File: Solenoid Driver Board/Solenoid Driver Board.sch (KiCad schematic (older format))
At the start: 21 parts, among them J1 BREAKOUT, J2 Solenoid, J3 RGB_LED, J4 DEBUG, J5 MAIN, Q1 IRLB8721PBF, U1 AMS1117-5.0, U2 STM8S003F3P, Y1 Crystal

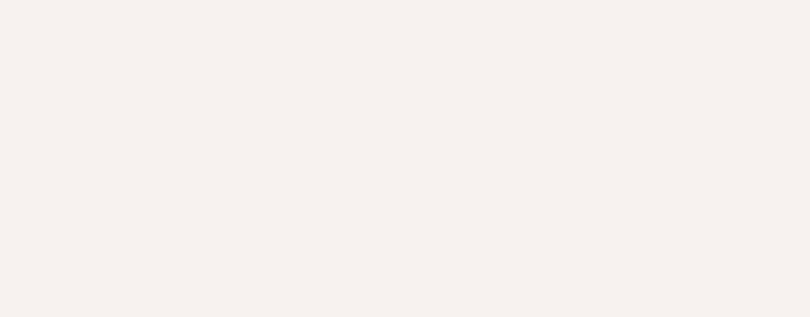
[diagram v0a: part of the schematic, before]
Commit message: Initial thoughts on protocol.  Initial board redesign notes.  Added libraries for firmware development
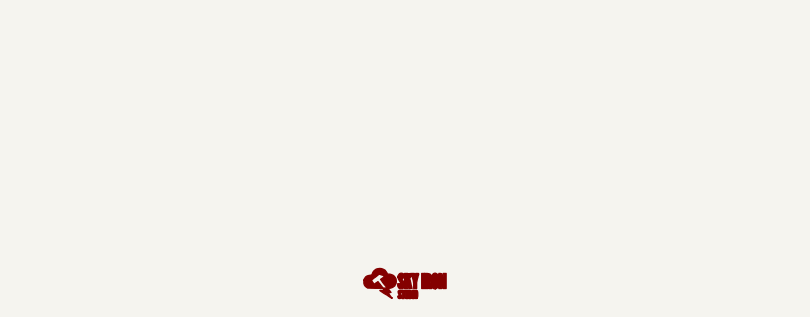
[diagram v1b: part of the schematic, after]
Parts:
- J3: footprint (none) -> Pin_Headers:Pin_Header_Straight_1x03
- R2, R4: footprint Resistors_SMD:R_0805_HandSoldering -> Resistors_SMD:R_1206_HandSoldering
- Y1: footprint Crystals:Crystal_SMD_2012-2pin_2.0x1.2mm_HandSoldering -> SpadeConnector:Crystal_HC-49-S
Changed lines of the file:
@@
 LIBS:diode
 LIBS:motors
+LIBS:SKyIronLogo
 LIBS:Solenoid Driver Board-cache
 EELAYER 25 0
@@
 $EndComp
 $Comp
-L +12V #PWR1
+L +12V #PWR01
 U 1 1 58F576B7
 P 2100 1400
-F 0 "#PWR1" H 2100 1250 50  0001 C CNN
+F 0 "#PWR01" H 2100 1250 50  0001 C CNN
 F 1 "+12V" H 2100 1540 50  0000 C CNN
 F 2 "" H 2100 1400 50  0001 C CNN
@@
 $EndComp
 $Comp
-L +5V #PWR4
+L +5V #PWR02
 U 1 1 58F576D3
 P 3100 1400
-F 0 "#PWR4" H 3100 1250 50  0001 C CNN
+F 0 "#PWR02" H 3100 1250 50  0001 C CNN
 F 1 "+5V" H 3100 1540 50  0000 C CNN
 F 2 "" H 3100 1400 50  0001 C CNN
@@
 $EndComp
 $Comp
-L GND #PWR3
+L GND #PWR03
 U 1 1 58F576F3
 P 2600 1850
-F 0 "#PWR3" H 2600 1600 50  0001 C CNN
+F 0 "#PWR03" H 2600 1600 50  0001 C CNN
 F 1 "GND" H 2600 1700 50  0000 C CNN
 F 2 "" H 2600 1850 50  0001 C CNN
@@
 	2900 1400 3500 1400
 $Comp
-L +5V #PWR6
+L +5V #PWR04
 U 1 1 58F5771C
 P 5200 1600
-F 0 "#PWR6" H 5200 1450 50  0001 C CNN
+F 0 "#PWR04" H 5200 1450 50  0001 C CNN
 F 1 "+5V" H 5200 1740 50  0000 C CNN
 F 2 "" H 5200 1600 50  0001 C CNN
@@
 $EndComp
 $Comp
-L GND #PWR7
+L GND #PWR05
 U 1 1 58F57736
 P 5200 3650
-F 0 "#PWR7" H 5200 3400 50  0001 C CNN
+F 0 "#PWR05" H 5200 3400 50  0001 C CNN
 F 1 "GND" H 5200 3500 50  0000 C CNN
 F 2 "" H 5200 3650 50  0001 C CNN
@@
 SWIM
 $Comp
-L GND #PWR18
+L GND #PWR06
 U 1 1 58F57AF4
 P 9950 1300
-F 0 "#PWR18" H 9950 1050 50  0001 C CNN
+F 0 "#PWR06" H 9950 1050 50  0001 C CNN
 F 1 "GND" H 9950 1150 50  0000 C CNN
 F 2 "" H 9950 1300 50  0001 C CNN
@@
 $EndComp
 $Comp
-L +5V #PWR17
+L +5V #PWR07
 U 1 1 58F57B17
 P 9950 1100
-F 0 "#PWR17" H 9950 950 50  0001 C CNN
+F 0 "#PWR07" H 9950 950 50  0001 C CNN
 F 1 "+5V" H 9950 1240 50  0000 C CNN
 F 2 "" H 9950 1100 50  0001 C CNN
@@
 F 0 "Y1" H 7150 2300 50  0000 C CNN
 F 1 "Crystal" H 7150 2000 50  0000 C CNN
-F 2 "Crystals:Crystal_SMD_2012-2pin_2.0x1.2mm_HandSoldering" H 7150 2150 50  0001 C CNN
+F 2 "SpadeConnector:Crystal_HC-49-S" H 7150 2150 50  0001 C CNN
 F 3 "" H 7150 2150 50  0001 C CNN
 	1    7150 2150
@@
 $EndComp
 $Comp
-L GND #PWR10
+L GND #PWR08
 U 1 1 58F57DD6
 P 7800 2150
-F 0 "#PWR10" H 7800 1900 50  0001 C CNN
+F 0 "#PWR08" H 7800 1900 50  0001 C CNN
 F 1 "GND" H 7800 2000 50  0000 C CNN
 F 2 "" H 7800 2150 50  0001 C CNN
@@
 $EndComp
 $Comp
-L GND #PWR14
+L GND #PWR09
 U 1 1 58F58125
 P 8750 4250
-F 0 "#PWR14" H 8750 4000 50  0001 C CNN
+F 0 "#PWR09" H 8750 4000 50  0001 C CNN
 F 1 "GND" H 8750 4100 50  0000 C CNN
 F 2 "" H 8750 4250 50  0001 C CNN
@@
 F 0 "R4" V 8680 4100 50  0000 C CNN
 F 1 "10K" V 8600 4100 50  0000 C CNN
-F 2 "Resistors_SMD:R_0805_HandSoldering" V 8530 4100 50  0001 C CNN
+F 2 "Resistors_SMD:R_1206_HandSoldering" V 8530 4100 50  0001 C CNN
 F 3 "" H 8600 4100 50  0001 C CNN
 	1    8600 4100
@@
 $EndComp
 $Comp
-L +12V #PWR13
+L +12V #PWR010
 U 1 1 58F5833A
 P 8750 3150
-F 0 "#PWR13" H 8750 3000 50  0001 C CNN
+F 0 "#PWR010" H 8750 3000 50  0001 C CNN
 F 1 "+12V" H 8750 3290 50  0000 C CNN
 F 2 "" H 8750 3150 50  0001 C CNN
@@
 $EndComp
 $Comp
-L +12V #PWR15
+L +12V #PWR011
 U 1 1 58F586EE
 P 9900 2050
-F 0 "#PWR15" H 9900 1900 50  0001 C CNN
+F 0 "#PWR011" H 9900 1900 50  0001 C CNN
 F 1 "+12V" H 9900 2190 50  0000 C CNN
 F 2 "" H 9900 2050 50  0001 C CNN
@@
 $EndComp
 $Comp
-L GND #PWR16
+L GND #PWR012
 U 1 1 58F58726
 P 9900 2150
-F 0 "#PWR16" H 9900 1900 50  0001 C CNN
+F 0 "#PWR012" H 9900 1900 50  0001 C CNN
 F 1 "GND" H 9900 2000 50  0000 C CNN
 F 2 "" H 9900 2150 50  0001 C CNN
@@
 F 0 "R2" V 2430 2650 50  0000 C CNN
 F 1 "10k" V 2350 2650 50  0000 C CNN
-F 2 "Resistors_SMD:R_0805_HandSoldering" V 2280 2650 50  0001 C CNN
+F 2 "Resistors_SMD:R_1206_HandSoldering" V 2280 2650 50  0001 C CNN
 F 3 "" H 2350 2650 50  0001 C CNN
 	1    2350 2650
@@
 $EndComp
 $Comp
-L +5V #PWR2
+L +5V #PWR013
 U 1 1 58FB95C2
 P 2350 2400
-F 0 "#PWR2" H 2350 2250 50  0001 C CNN
+F 0 "#PWR013" H 2350 2250 50  0001 C CNN
 F 1 "+5V" H 2350 2540 50  0000 C CNN
 F 2 "" H 2350 2400 50  0001 C CNN
@@
 Connection ~ 2100 1400
 $Comp
-L GND #PWR5
+L GND #PWR014
 U 1 1 58FBA70F
 P 3100 1850
-F 0 "#PWR5" H 3100 1600 50  0001 C CNN
+F 0 "#PWR014" H 3100 1600 50  0001 C CNN
 F 1 "GND" H 3100 1700 50  0000 C CNN
 F 2 "" H 3100 1850 50  0001 C CNN
@@
 $EndComp
 $Comp
-L +5V #PWR11
+L +5V #PWR015
 U 1 1 5903B528
 P 8400 1100
-F 0 "#PWR11" H 8400 950 50  0001 C CNN
+F 0 "#PWR015" H 8400 950 50  0001 C CNN
 F 1 "+5V" H 8400 1240 50  0000 C CNN
 F 2 "" H 8400 1100 50  0001 C CNN
@@
 $EndComp
 $Comp
-L GND #PWR12
+L GND #PWR016
 U 1 1 5903B57B
 P 8400 1600
-F 0 "#PWR12" H 8400 1350 50  0001 C CNN
+F 0 "#PWR016" H 8400 1350 50  0001 C CNN
 F 1 "GND" H 8400 1450 50  0000 C CNN
 F 2 "" H 8400 1600 50  0001 C CNN
@@
 F 0 "J3" H 7050 3500 50  0000 C CNN
 F 1 "RGB_LED" V 7150 3300 50  0000 C CNN
-F 2 "" H 7050 3300 50  0001 C CNN
+F 2 "Pin_Headers:Pin_Header_Straight_1x03" H 7050 3300 50  0001 C CNN
 F 3 "" H 7050 3300 50  0001 C CNN
 	1    7050 3300
@@
 	6500 3200 6850 3200
 $Comp
-L +5V #PWR8
+L +5V #PWR017
 U 1 1 5904B931
 P 6850 3300
-F 0 "#PWR8" H 6850 3150 50  0001 C CNN
+F 0 "#PWR017" H 6850 3150 50  0001 C CNN
 F 1 "+5V" H 6850 3440 50  0000 C CNN
 F 2 "" H 6850 3300 50  0001 C CNN
@@
 $EndComp
 $Comp
-L GND #PWR9
+L GND #PWR018
 U 1 1 5904B984
 P 6850 3400
-F 0 "#PWR9" H 6850 3150 50  0001 C CNN
+F 0 "#PWR018" H 6850 3150 50  0001 C CNN
 F 1 "GND" H 6850 3250 50  0000 C CNN
 F 2 "" H 6850 3400 50  0001 C CNN
@@
 	0    1    1    0
 $EndComp
+$Comp
+L LOGO #G?
+U 1 1 59053450
+P 6300 5900
+F 0 "#G?" H 6300 5864 60  0001 C CNN
+F 1 "LOGO" H 6300 5936 60  0001 C CNN
+F 2 "" H 6300 5900 60  0001 C CNN
+F 3 "" H 6300 5900 60  0001 C CNN
+	1    6300 5900
+	1    0    0    -1
+$EndComp
 $EndSCHEMATC

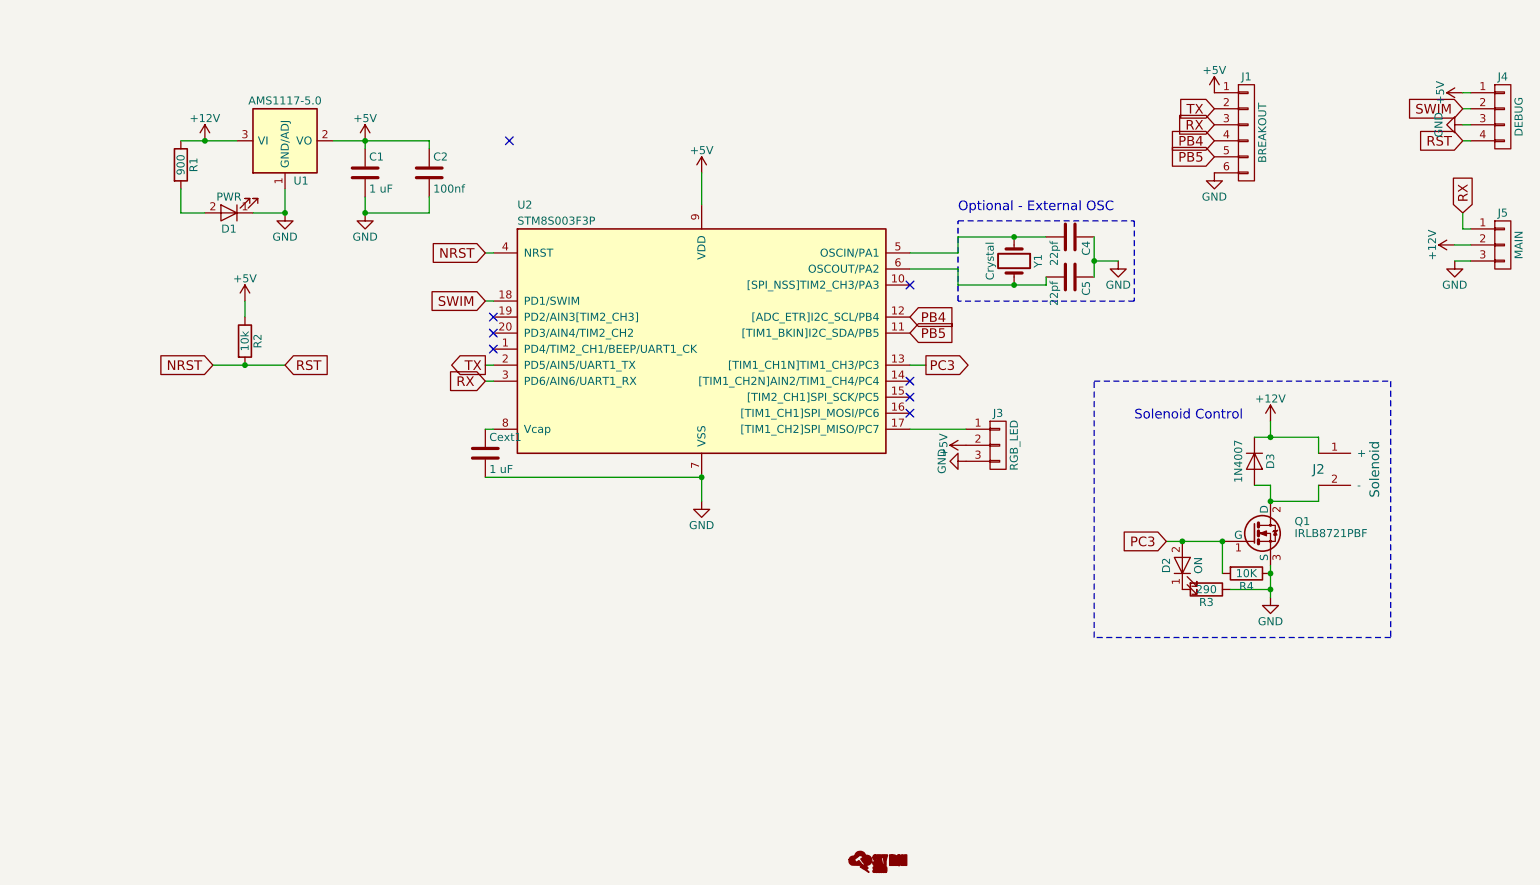
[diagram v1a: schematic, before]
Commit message: Moved fade to TIM4, started work on new board revision
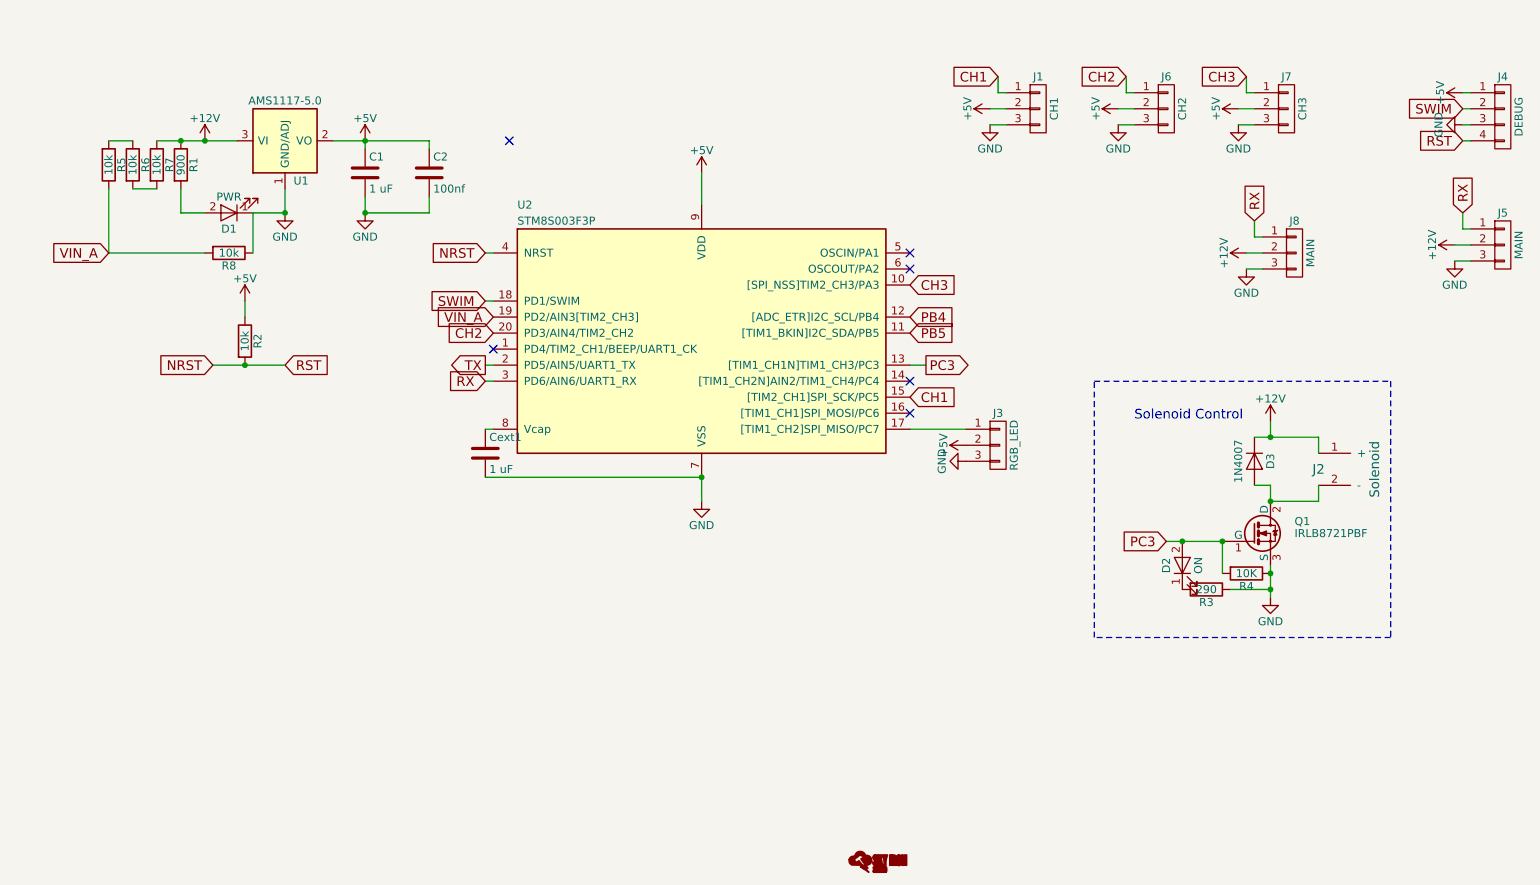
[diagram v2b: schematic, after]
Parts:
- removed C4, C5: 22pf, Capacitors_SMD:C_1206_HandSoldering, symbol C
- removed J1: BREAKOUT, Pin_Headers:Pin_Header_Straight_1x06_Pitch2.54mm, symbol CONN_01X06
- removed Y1: Crystal, SpadeConnector:Crystal_HC-49-S, symbol Crystal
- added J1: CH1, Pin_Headers:Pin_Header_Straight_1x03_Pitch2.54mm, symbol CONN_01X03
- added J6: CH2, Pin_Headers:Pin_Header_Straight_1x03_Pitch2.54mm, symbol CONN_01X03
- added J7: CH3, Pin_Headers:Pin_Header_Straight_1x03_Pitch2.54mm, symbol CONN_01X03
- added J8: MAIN, Pin_Headers:Pin_Header_Straight_1x03_Pitch2.54mm, symbol CONN_01X03
- added R5, R6, R7, R8: 10k, Resistors_SMD:R_0805_HandSoldering, symbol R
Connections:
- net +12V: now also J8.2 (P2), R7.1
- net +5V: now also J1.2 (P2), J6.2 (P2), J7.2 (P2)
- net GND: now also J1.3 (P3), J6.3 (P3), J7.3 (P3), J8.3 (P3), R8.1
- net RX: now also J8.1 (P1)
- net CH3: now reaches U2.10 ([SPI_NSS]TIM2_CH3/PA3)
- net CH3: now also J7.1 (P1)
- net CH1: now reaches U2.15 ([TIM2_CH1]SPI_SCK/PC5)
- net CH1: now also J1.1 (P1)
- net VIN_A: now reaches U2.19 (PD2/AIN3[TIM2_CH3])
- net VIN_A: now also R5.1, R8.2
- net CH2: now reaches U2.20 (PD3/AIN4/TIM2_CH2)
- net CH2: now also J6.1 (P1)
- new net: R6.2, R7.2
- new net: R5.2, R6.1
- no-connect marks 8 -> 6
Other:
- note removed: "Optional - External OSC"
